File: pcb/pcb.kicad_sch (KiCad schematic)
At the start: 4 parts, among them J1 Conn_01x05_Pin, J2 Conn_01x16_Pin, J3 Conn_01x05_Pin

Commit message: Pcb schematic done
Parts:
- added RV1: R_Potentiometer, symbol Device:R_Potentiometer
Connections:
- net 5v is gone; now on net +5V: J2.2 (Pin_2)
- net gnd1 is gone; now on net GND: J2.1 (Pin_1)
- net gnd2 is gone; now on net GND: J2.5 (Pin_5)
- net d2: now also A1.17 (D2)
- net d3: now also A1.18 (D3)
- net d4: now also A1.19 (D4)
- net d5: now also A1.20 (D5)
- net d6: now also A1.21 (D6)
- net d7: now also A1.22 (D7)
- net +5V: now reaches J2.15 (Pin_15)
- net +5V: now also A1.5 (+5V), RV1.1
- net GND: now reaches J2.16 (Pin_16)
- net GND: now also A1.29 (GND), A1.6 (GND), A1.7 (GND), RV1.3
- net poten: now reaches J2.3 (Pin_3)
- net poten: now also RV1.2
- net at A1.31 (SDA/A4): no longer A1.32 (SCL/A5)
- net +3.3V: now reaches A1.4 (3V3)
- no-connect marks 0 -> 14

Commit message: pcb 1
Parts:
- J1, J3: footprint (none) -> Connector_PinHeader_2.54mm:PinHeader_1x05_P2.54mm_Vertical
- J2: footprint (none) -> Connector_PinHeader_2.54mm:PinHeader_1x16_P2.54mm_Vertical
- RV1: footprint (none) -> Potentiometer_THT:Potentiometer_Alpha_RD901F-40-00D_Single_Vertical
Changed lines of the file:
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@@
 			)
 		)
-		(property "Footprint" ""
+		(property "Footprint" "Connector_PinHeader_2.54mm:PinHeader_1x05_P2.54mm_Vertical"
 			(at 208.28 63.5 0)
 			(effects
@@
 			)
 		)
-		(property "Footprint" ""
+		(property "Footprint" "Connector_PinHeader_2.54mm:PinHeader_1x16_P2.54mm_Vertical"
 			(at 60.96 163.83 0)
 			(effects
@@
 			)
 		)
-		(property "Footprint" ""
+		(property "Footprint" "Potentiometer_THT:Potentiometer_Alpha_RD901F-40-00D_Single_Vertical"
 			(at 132.08 138.43 0)
 			(effects
@@
 			)
 		)
-		(property "Footprint" ""
+		(property "Footprint" "Connector_PinHeader_2.54mm:PinHeader_1x05_P2.54mm_Vertical"
 			(at 195.58 77.47 0)
 			(effects

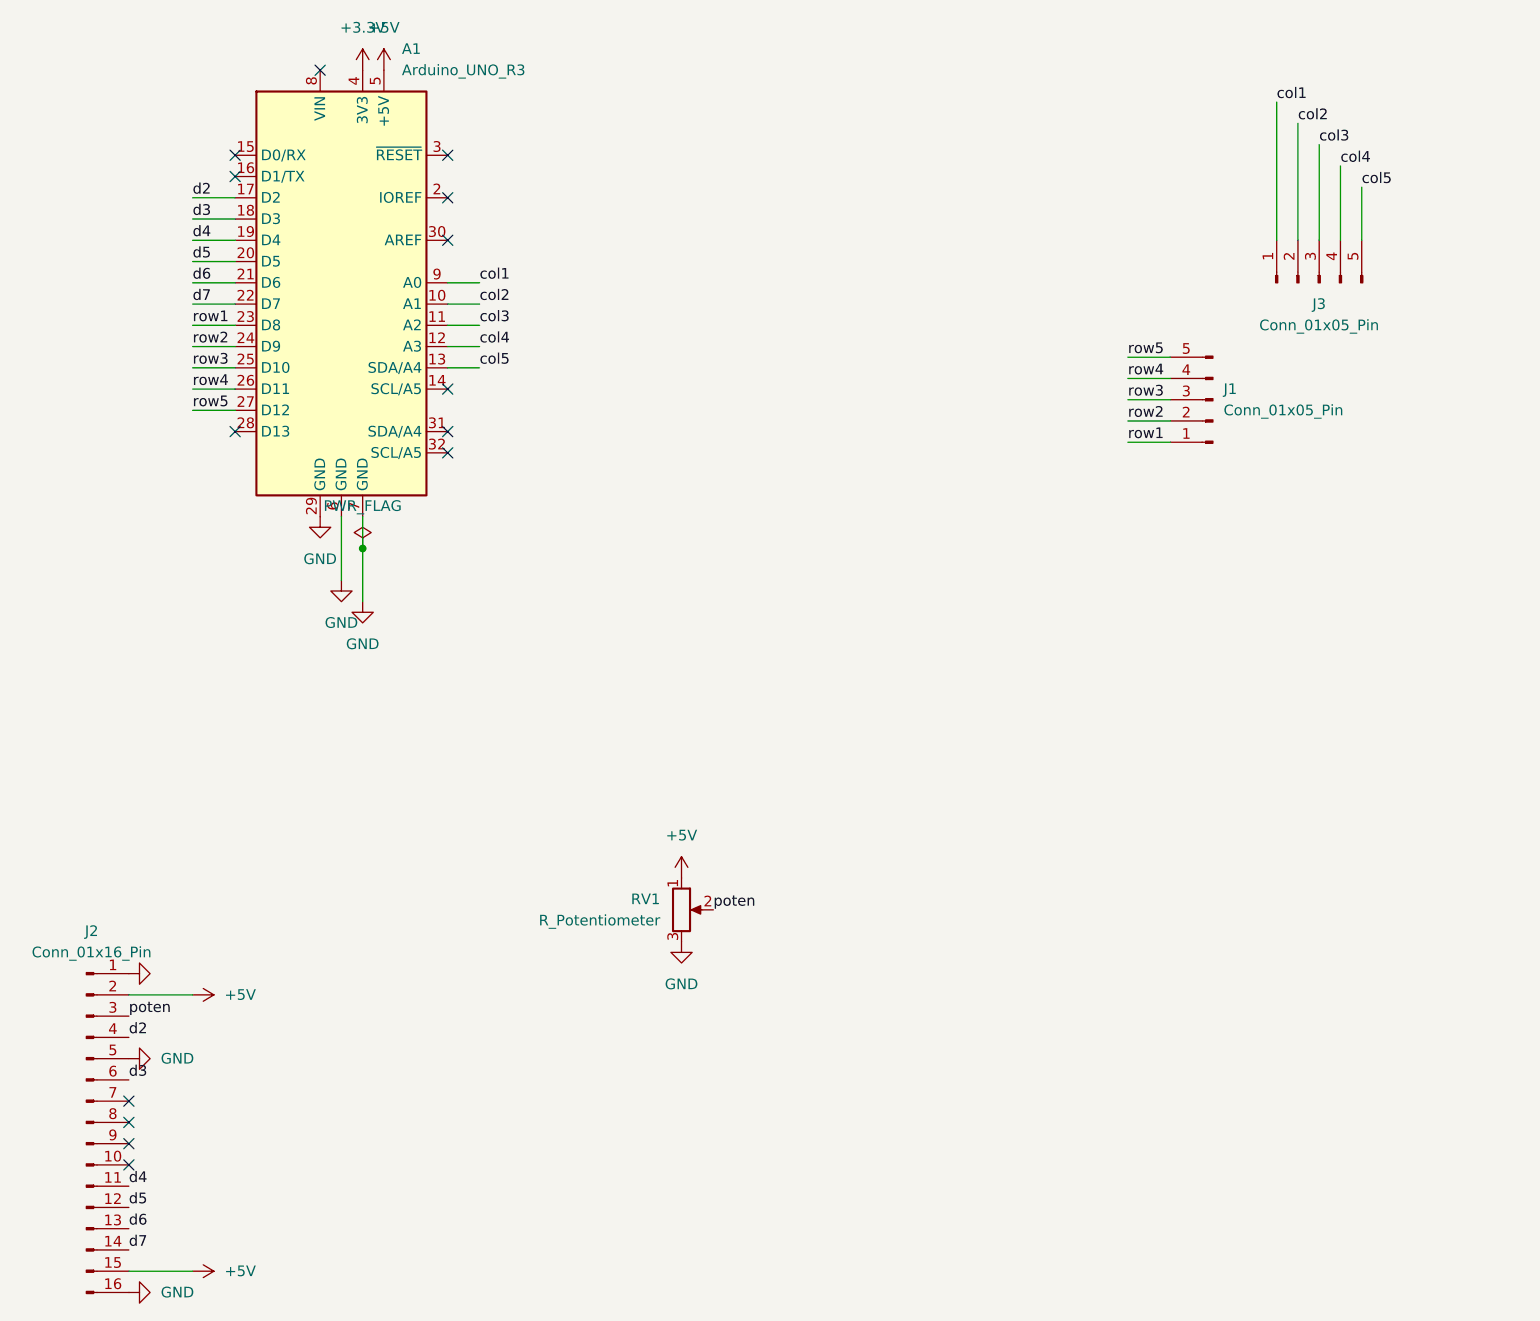
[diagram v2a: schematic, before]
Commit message: sch with button
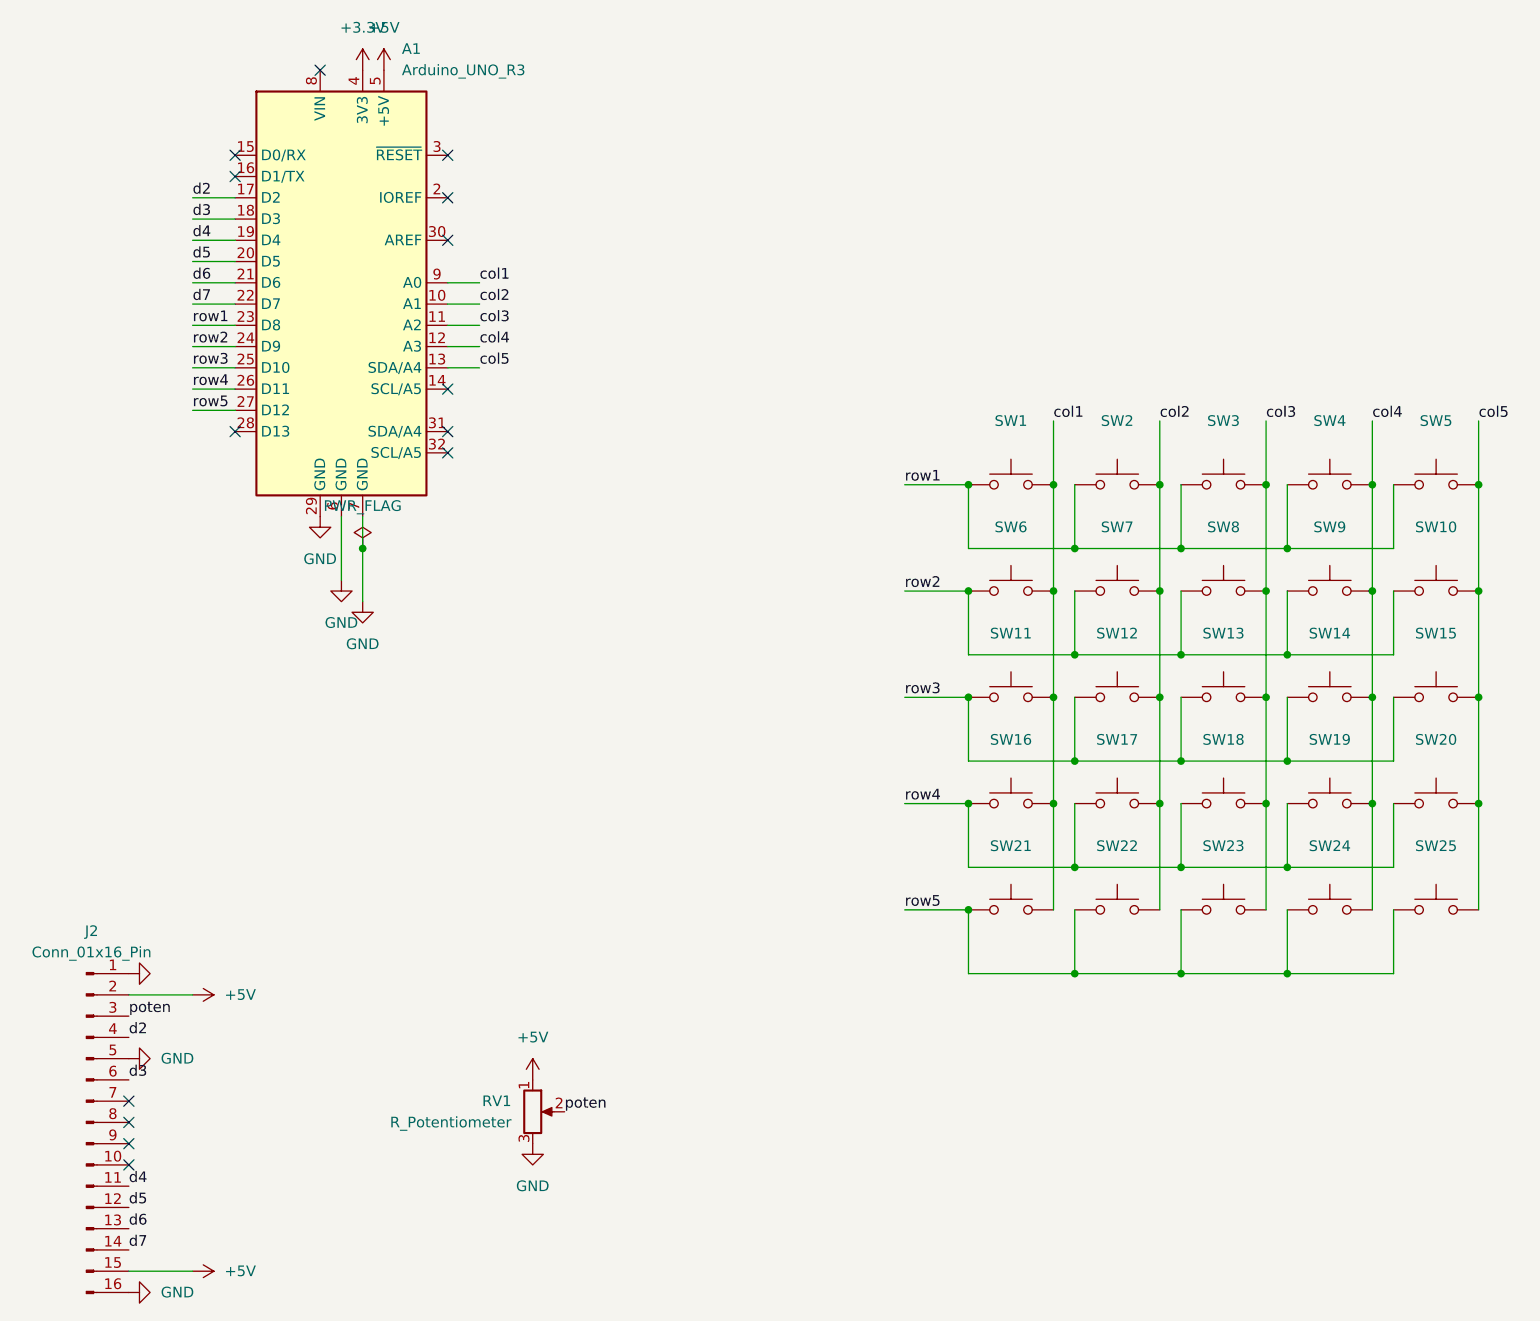
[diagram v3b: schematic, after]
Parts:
- removed J1, J3: Conn_01x05_Pin, Connector_PinHeader_2.54mm:PinHeader_1x05_P2.54mm_Vertical, symbol Connector:Conn_01x05_Pin
- added SW1, SW10, SW11, SW12, SW13, SW14, SW15, SW16, SW17, SW18, SW19, SW2, SW20, SW21, SW22, SW23, SW24, SW25, SW3, SW4, SW5, SW6, SW7, SW8, SW9: SW_Push, Button_Switch_THT:SW_PUSH_6mm, symbol Switch:SW_Push
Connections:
- net col1: now also SW1.2, SW11.2, SW16.2, SW21.2, SW6.2
- net col2: now also SW12.2, SW17.2, SW2.2, SW22.2, SW7.2
- net col3: now also SW13.2, SW18.2, SW23.2, SW3.2, SW8.2
- net col4: now also SW14.2, SW19.2, SW24.2, SW4.2, SW9.2
- net col5: now also SW10.2, SW15.2, SW20.2, SW25.2, SW5.2
- net row1: now also SW1.1, SW2.1, SW3.1, SW4.1, SW5.1
- net row2: now also SW10.1, SW6.1, SW7.1, SW8.1, SW9.1
- net row3: now also SW11.1, SW12.1, SW13.1, SW14.1, SW15.1
- net row4: now also SW16.1, SW17.1, SW18.1, SW19.1, SW20.1
- net row5: now also SW21.1, SW22.1, SW23.1, SW24.1, SW25.1
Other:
- moved on the sheet: RV1
